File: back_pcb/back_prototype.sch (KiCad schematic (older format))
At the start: 87 parts, among them P1 EXPANSION_LEFT, P2 EXPANSION_BOTTOM, P3 EXPANSION_TOP, P4 USB_A, P5 AUDIO_CONN, P6 ATMEGA_HEADER, P7 EXPANSION_BOTTOM2, P8 JST, Q1 IRLML6401, Q2 BSS138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

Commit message: Back board almost finished - lots of changes
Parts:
- removed C7: 100nF, Capacitors_SMD:C_0805, symbol C_Small
- removed JP7: 3V3/5V, Connect:GS3, symbol JUMPER3
- removed JP8: CA/CC, Connect:GS3, symbol JUMPER3
- removed P2: EXPANSION_BOTTOM, Pin_Headers:Pin_Header_Angled_1x04_Pitch2.54mm, symbol CONN_01X04
- removed Q2, Q3: BSS138, TO_SOT_Packages_SMD:SOT-23_Handsoldering, symbol Q_NMOS_GSD
- removed R8, R9: 10K, Resistors_SMD:R_0805_HandSoldering, symbol R
- removed W16, W21, W22, W23, W24: TEST_1P, Measurement_Points:Measurement_Point_Square-SMD-Pad_Small, symbol TEST_1P
- added JP7: Jumper_NC_Small, common-footprints:GS2_SMALL, symbol Jumper_NC_Small
- added P2: EXPANSION_BOTTOM, Pin_Headers:Pin_Header_Angled_1x05_Pitch2.54mm, symbol CONN_01X05
- C1, C2: renamed from C?; footprint Capacitors_SMD:C_0805 -> Capacitors_SMD:C_0805_HandSoldering
- C13, C14, C15, C25, C5, C6, C8: footprint Capacitors_SMD:C_0805 -> Capacitors_SMD:C_0805_HandSoldering
- C16, C17, C18, C19, C20, C21, C22, C23, C24: footprint Capacitors_SMD:C_0603 -> Capacitors_SMD:C_0603_HandSoldering
- JP10, JP2, JP9: footprint Connect:GS2 -> common-footprints:GS2_SMALL
- JP11, JP12: renamed from JP?; footprint Connect:GS2 -> common-footprints:GS2_SMALL
- JP3, JP4, JP6: footprint Connect:GS3 -> common-footprints:GS3_SMALL
- P4: footprint Connect:USB_A -> footprints:USB_A
- P6: footprint (none) -> Pin_Headers:Pin_Header_Straight_1x06_Pitch2.54mm
- P7: footprint (none) -> Pin_Headers:Pin_Header_Angled_1x03_Pitch2.54mm
- P9: renamed from P?; footprint Connect:USB_A -> footprints:USB_A
- U3: footprint SMD_Packages:SOIC-28 -> Housings_SOIC:SOIC-28W_7.5x17.9mm_Pitch1.27mm
- gave numbers to parts that had none: 1
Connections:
- net labels added: ATMEGA_R_G, BH_GPIO_1, LH_GPIO_4
- net labels removed: ATMEGA_GPIO, ATMEGA_R/G, BH_GPIO
- wire segments 112 -> 87
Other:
- note added: "Small headers with I2C, 3.3V,\n+5V, one GPIO and one ADC. \nCan be useful for small \nanalog and I2C sensors."
- note removed: "A nice notification LED footprint -\nallowing both common-cathode\nand common-anode LEDs,\nwhatever's handy."
- note removed: "Small headers with I2C, 3.3V,\nVBAT, one GPIO and one ADC. \nCan be useful for small \nanalog and I2C sensors."
- note removed: "This RTC footprint supports both 3.3V and 5V RTCs\n(with level shifting footprints for the latter case,\nby default level shifting is disabled with jumpers.)"
- moved on the sheet: C13, C14, C15, C25, C6, D3, JP10, JP2, JP9, R5, R6, R7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

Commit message: Updated TODO and schematic clarifications
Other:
- note added: "Big expansion header \nwith SPI, 4 GPIOs, \nwith I2S/SPI alt f.,\n5V/3.3V and TV-OUT."
- note added: "Small headers with I2C, 3.3V,\n+5V, one GPIO, VIN and ADC. \nCan be useful for small \nanalog and I2C sensors."
- note removed: "Big expansion header \nwith SPI, 2 GPIOs, \nvarious voltages and \nanalog video out.\nAlso has 5V charger \ninput and 5V DC-DC out."
- note removed: "Small headers with I2C, 3.3V,\n+5V, one GPIO and one ADC. \nCan be useful for small \nanalog and I2C sensors."
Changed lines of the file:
@@
 SDA
 Text Notes 4850 7450 0    60   ~ 0
-Small headers with I2C, 3.3V,\n+5V, one GPIO and one ADC. \nCan be useful for small \nanalog and I2C sensors.
+Small headers with I2C, 3.3V,\n+5V, one GPIO, VIN and ADC. \nCan be useful for small \nanalog and I2C sensors.
 Text GLabel 950  4900 0    60   Input ~ 0
 TV_OUT
@@
 LH_GPIO_2
 Text Notes 3150 6300 0    60   ~ 0
-Big expansion header \nwith SPI, 2 GPIOs, \nvarious voltages and \nanalog video out.\nAlso has 5V charger \ninput and 5V DC-DC out.
+Big expansion header \nwith SPI, 4 GPIOs, \nwith I2S/SPI alt f.,\n5V/3.3V and TV-OUT.
 $Comp
 L CONN_01X13 P1

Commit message: Cleared up ground, removed testpoints
Removed some ground and I2C GPIO expander testpoints
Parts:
- removed W12: GND, Measurement_Points:Measurement_Point_Square-SMD-Pad_Small, symbol TEST_1P
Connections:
- net +3V3: now also JP7.1, U5.5 (VCC)
- net RTC_ALARM: now also JP2.1, U5.6 (SQW)
- net SCL: now also JP9.1, U5.7 (SCL)
- net SDA: now also JP10.1, U5.8 (SDA)
- no-connect marks 20 -> 26
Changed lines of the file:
@@
-$EndComp
-$Comp
-L TEST_1P W12
-U 1 1 5845AF6D
-P 4100 3400
-F 0 "W12" V 4150 3450 50  0000 C CNN
-F 1 "GND" V 4100 3650 50  0000 C CNN
-F 2 "Measurement_Points:Measurement_Point_Square-SMD-Pad_Small" H 4300 3400 50  0001 C CNN
-F 3 "" H 4300 3400 50  0000 C CNN
-	1    4100 3400
-	0    -1   -1   0
 $EndComp
 $Comp
@@
 Text GLabel 3550 5200 2    60   Input ~ 0
 IR_RX
-$Comp
-L GND #PWR051
-U 1 1 58906F99
-P 4100 3400
-F 0 "#PWR051" H 4100 3150 50  0001 C CNN
-F 1 "GND" H 4100 3250 50  0000 C CNN
-F 2 "" H 4100 3400 50  0000 C CNN
-F 3 "" H 4100 3400 50  0000 C CNN
-	1    4100 3400
-	0    -1   -1   0
-$EndComp
 Text GLabel 950  4800 0    60   Input ~ 0
 PI_RST
@@
 BATT-
 $Comp
-L +BATT #PWR052
+L +BATT #PWR051
 U 1 1 5891128C
 P 6600 6300
-F 0 "#PWR052" H 6600 6150 50  0001 C CNN
+F 0 "#PWR051" H 6600 6150 50  0001 C CNN
 F 1 "+BATT" V 6600 6550 50  0000 C CNN
 F 2 "" H 6600 6300 50  0000 C CNN
@@
 $EndComp
 $Comp
-L +BATT #PWR053
+L +BATT #PWR052
 U 1 1 5890509D
 P 7600 6200
-F 0 "#PWR053" H 7600 6050 50  0001 C CNN
+F 0 "#PWR052" H 7600 6050 50  0001 C CNN
 F 1 "+BATT" V 7500 6300 50  0000 C CNN
 F 2 "" H 7600 6200 50  0000 C CNN
@@
 DCDC_EN
 $Comp
-L GND #PWR054
+L GND #PWR053
 U 1 1 589066FA
 P 8300 6300
-F 0 "#PWR054" H 8300 6050 50  0001 C CNN
+F 0 "#PWR053" H 8300 6050 50  0001 C CNN
 F 1 "GND" V 8300 6100 50  0000 C CNN
 F 2 "" H 8300 6300 50  0000 C CNN
@@
 $EndComp
 $Comp
-L GND #PWR055
+L GND #PWR054
 U 1 1 58906807
 P 9150 6300
-F 0 "#PWR055" H 9150 6050 50  0001 C CNN
+F 0 "#PWR054" H 9150 6050 50  0001 C CNN
 F 1 "GND" V 9150 6100 50  0000 C CNN
 F 2 "" H 9150 6300 50  0000 C CNN
@@
 $EndComp
 $Comp
-L +5V #PWR056
+L +5V #PWR055
 U 1 1 58906E74
 P 9150 6400
-F 0 "#PWR056" H 9150 6250 50  0001 C CNN
+F 0 "#PWR055" H 9150 6250 50  0001 C CNN
 F 1 "+5V" V 9150 6600 50  0000 C CNN
 F 2 "" H 9150 6400 50  0000 C CNN
@@
 DCDC_EN
 $Comp
-L +BATT #PWR057
+L +BATT #PWR056
 U 1 1 58911AF4
 P 850 7250
-F 0 "#PWR057" H 850 7100 50  0001 C CNN
+F 0 "#PWR056" H 850 7100 50  0001 C CNN
 F 1 "+BATT" H 850 7450 50  0000 C CNN
 F 2 "" H 850 7250 50  0000 C CNN
@@
 $EndComp
 $Comp
-L +3.3V #PWR058
+L +3.3V #PWR057
 U 1 1 58914166
 P 7400 700
-F 0 "#PWR058" H 7400 550 50  0001 C CNN
+F 0 "#PWR057" H 7400 550 50  0001 C CNN
 F 1 "+3.3V" H 7550 800 50  0000 C CNN
 F 2 "" H 7400 700 50  0000 C CNN
@@
 $EndComp
 $Comp
-L GND #PWR059
+L GND #PWR058
 U 1 1 589168FA
 P 850 7500
-F 0 "#PWR059" H 850 7250 50  0001 C CNN
+F 0 "#PWR058" H 850 7250 50  0001 C CNN
 F 1 "GND" H 850 7350 50  0000 C CNN
 F 2 "" H 850 7500 50  0000 C CNN
@@
 $EndComp
 $Comp
-L GND #PWR060
+L GND #PWR059
 U 1 1 58C8C046
 P 2900 7500
-F 0 "#PWR060" H 2900 7250 50  0001 C CNN
+F 0 "#PWR059" H 2900 7250 50  0001 C CNN
 F 1 "GND" H 2900 7350 50  0000 C CNN
 F 2 "" H 2900 7500 50  0000 C CNN
@@
 $EndComp
 $Comp
-L +5V #PWR061
+L +5V #PWR060
 U 1 1 58C8C4CB
 P 2900 7200
-F 0 "#PWR061" H 2900 7050 50  0001 C CNN
+F 0 "#PWR060" H 2900 7050 50  0001 C CNN
 F 1 "+5V" H 2900 7350 50  0000 C CNN
 F 2 "" H 2900 7200 50  0000 C CNN
@@
 NoConn ~ 10850 4900
 $Comp
-L +5V #PWR062
+L +5V #PWR061
 U 1 1 58C96531
 P 10450 4400
-F 0 "#PWR062" H 10450 4250 50  0001 C CNN
+F 0 "#PWR061" H 10450 4250 50  0001 C CNN
 F 1 "+5V" V 10450 4600 50  0000 C CNN
 F 2 "" H 10450 4400 50  0000 C CNN
@@
 $EndComp
 $Comp
-L GND #PWR063
+L GND #PWR062
 U 1 1 58C96537
 P 10450 4700
-F 0 "#PWR063" H 10450 4450 50  0001 C CNN
+F 0 "#PWR062" H 10450 4450 50  0001 C CNN
 F 1 "GND" V 10450 4500 50  0000 C CNN
 F 2 "" H 10450 4700 50  0000 C CNN
@@
 	9350 1450 9250 1450
 $Comp
-L +BATT #PWR064
+L +BATT #PWR063
 U 1 1 58C95019
 P 9400 5000
-F 0 "#PWR064" H 9400 4850 50  0001 C CNN
+F 0 "#PWR063" H 9400 4850 50  0001 C CNN
 F 1 "+BATT" V 9400 5250 50  0000 C CNN
 F 2 "" H 9400 5000 50  0000 C CNN
@@
 	5250 6050 7000 6050
 $Comp
-L +BATT #PWR065
+L +BATT #PWR064
 U 1 1 58C9B79E
 P 6200 3250
-F 0 "#PWR065" H 6200 3100 50  0001 C CNN
+F 0 "#PWR064" H 6200 3100 50  0001 C CNN
 F 1 "+BATT" H 6200 3400 50  0000 C CNN
 F 2 "" H 6200 3250 50  0000 C CNN
@@
 $EndComp
 $Comp
-L +BATT #PWR066
+L +BATT #PWR065
 U 1 1 58C9B899
 P 5800 950
-F 0 "#PWR066" H 5800 800 50  0001 C CNN
+F 0 "#PWR065" H 5800 800 50  0001 C CNN
 F 1 "+BATT" H 5900 1100 50  0000 C CNN
 F 2 "" H 5800 950 50  0000 C CNN
@@
 $EndComp
 $Comp
-L +BATT #PWR067
+L +BATT #PWR066
 U 1 1 58CA03B3
 P 9350 700
-F 0 "#PWR067" H 9350 550 50  0001 C CNN
+F 0 "#PWR066" H 9350 550 50  0001 C CNN
 F 1 "+BATT" H 9450 850 50  0000 C CNN
 F 2 "" H 9350 700 50  0000 C CNN
@@
 	2850 2750 2700 2750
 $Comp
-L +BATT #PWR068
+L +BATT #PWR067
 U 1 1 58CB90A9
 P 5600 950
-F 0 "#PWR068" H 5600 800 50  0001 C CNN
+F 0 "#PWR067" H 5600 800 50  0001 C CNN
 F 1 "+BATT" H 5450 1000 50  0000 C CNN
 F 2 "" H 5600 950 50  0000 C CNN
@@
 $EndComp
 $Comp
-L +BATT #PWR069
+L +BATT #PWR068
 U 1 1 58CB91F4
 P 5600 2700
-F 0 "#PWR069" H 5600 2550 50  0001 C CNN
+F 0 "#PWR068" H 5600 2550 50  0001 C CNN
 F 1 "+BATT" H 5450 2750 50  0000 C CNN
 F 2 "" H 5600 2700 50  0000 C CNN
@@
 BH_GPIO_1
 $Comp
-L +5V #PWR070
+L +5V #PWR069
 U 1 1 58CBF7BB
 P 4950 6950
-F 0 "#PWR070" H 4950 6800 50  0001 C CNN
+F 0 "#PWR069" H 4950 6800 50  0001 C CNN
 F 1 "+5V" V 4950 7150 50  0000 C CNN
 F 2 "" H 4950 6950 50  0000 C CNN
@@
 	9950 3500 11200 3500
 $Comp
-L GND #PWR071
+L GND #PWR070
 U 1 1 58CC88F7
 P 950 5750
-F 0 "#PWR071" H 950 5500 50  0001 C CNN
+F 0 "#PWR070" H 950 5500 50  0001 C CNN
 F 1 "GND" H 950 5600 50  0000 C CNN
 F 2 "" H 950 5750 50  0000 C CNN
@@
 LH_GPIO_4
 NoConn ~ 6400 1850
+NoConn ~ 5150 1850
+NoConn ~ 5150 1750
+NoConn ~ 5150 1650
+NoConn ~ 5150 1550
+NoConn ~ 5150 1450
+NoConn ~ 5150 1350
+Wire Wire Line
+	9350 1450 9350 1400
+Wire Wire Line
+	9350 1400 9550 1400
+Wire Wire Line
+	9550 1400 9550 1450
+Connection ~ 9550 1450
+Connection ~ 9350 1450
+Wire Wire Line
+	9850 1550 9850 1500
+Wire Wire Line
+	9850 1500 9250 1500
+Wire Wire Line
+	9250 1500 9250 1550
+Connection ~ 9250 1550
+Connection ~ 9850 1550
+Wire Wire Line
+	9900 1650 9900 1700
+Wire Wire Line
+	9900 1700 10100 1700
+Wire Wire Line
+	10100 1700 10100 1650
+Wire Wire Line
+	10150 1750 10150 1800
+Wire Wire Line
+	10150 1800 10350 1800
+Wire Wire Line
+	10350 1800 10350 1750
+Connection ~ 10350 1750
+Connection ~ 10150 1750
+Connection ~ 10100 1650
+Connection ~ 9900 1650
 $EndSCHEMATC

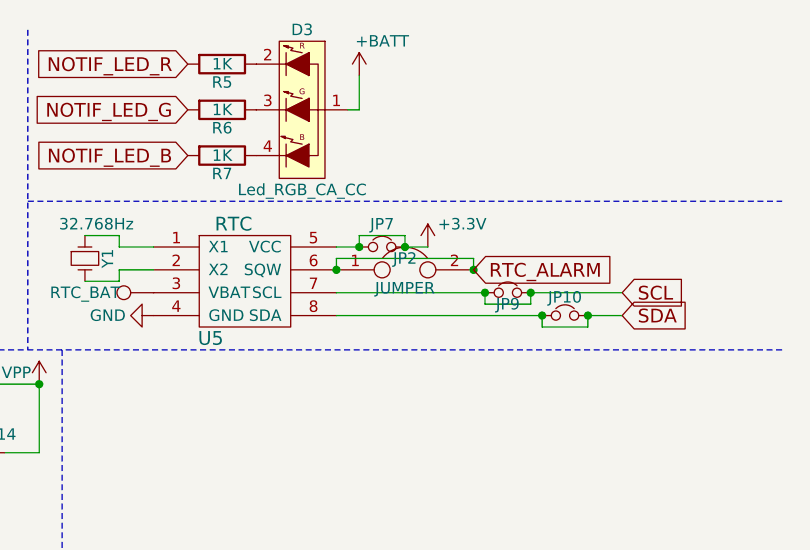
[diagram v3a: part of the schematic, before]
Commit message: Final changes
* Added fiducials
* Modified footprints to have bigger holes
* Added OSHW logo, release information and references
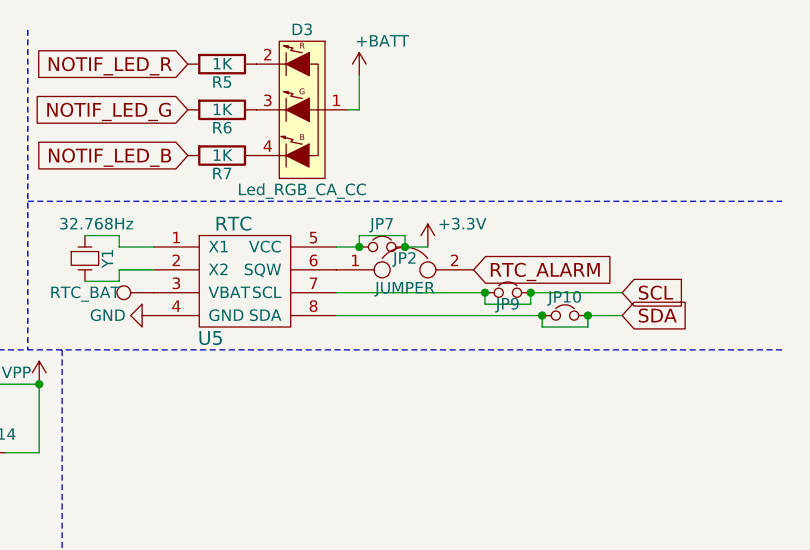
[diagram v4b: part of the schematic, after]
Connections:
- net RTC_ALARM: no longer JP2.1, U5.6 (SQW)
- new net: JP2.1, U5.6 (SQW)
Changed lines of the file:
@@
 Connection ~ 9350 1450
-Wire Wire Line
-	9850 1550 9850 1500
-Wire Wire Line
-	9850 1500 9250 1500
-Wire Wire Line
-	9250 1500 9250 1550
-Connection ~ 9250 1550
-Connection ~ 9850 1550
 Wire Wire Line
 	9900 1650 9900 1700
